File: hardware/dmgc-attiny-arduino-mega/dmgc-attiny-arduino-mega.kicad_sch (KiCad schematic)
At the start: 36 parts, among them J1 Power, J2 Analog, J3 Analog, J4 Digital, J5 PWM, J6 PWM, J7 Communication, SW1 Toggle Flash / Run, SW2 SELECT, SW3 RIGHT, SW4 LEFT, SW5 PUSH, SW6 START/RESET, U1 ATtiny85-20P, U2 Mutex

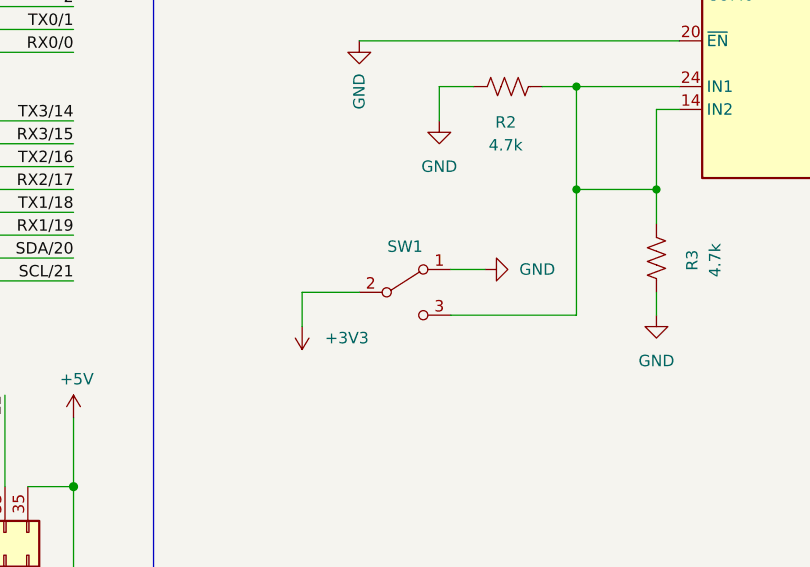
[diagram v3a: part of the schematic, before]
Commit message: Updated gerbers to v0.4, fixed switch problem with pins reversed. Moved C2 to a better location. Added labels for switch.
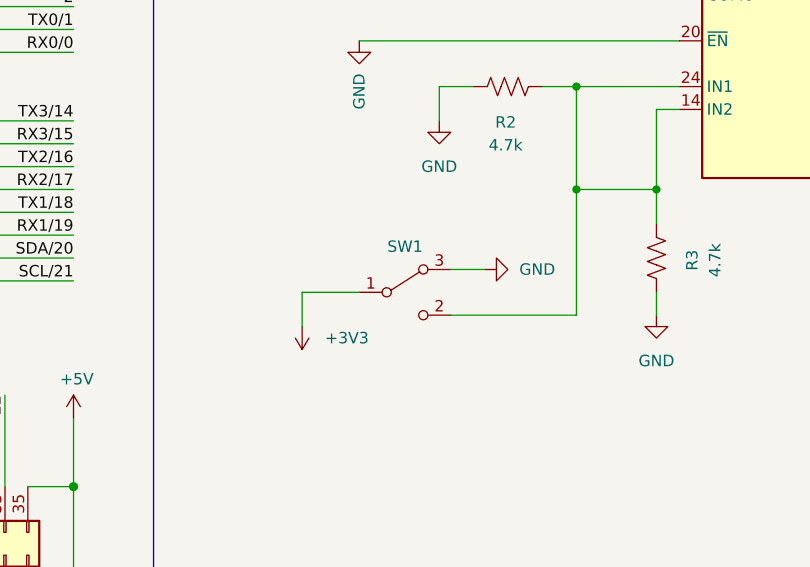
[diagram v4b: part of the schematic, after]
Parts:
- C1, C2, C3: footprint Capacitor_SMD:C_0201_0603Metric -> Capacitor_SMD:C_0603_1608Metric
- R1, R10, R2, R3, R4, R5, R6, R7, R8, R9: footprint Resistor_SMD:R_0201_0603Metric -> Resistor_SMD:R_0603_1608Metric
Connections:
- net +3V3: now also SW1.1 (B); no longer SW1.2 (B)
- net GND: now also SW1.3 (A); no longer SW1.1 (A)
- net at R2.2, R3.2, U2.14 (IN2)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: now also SW1.2 (C); no longer SW1.3 (C)
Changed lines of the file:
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@@
     (title "DMGC Arduino Mega 2650 Shield")
     (date "mar. 31 mars 2015")
-    (rev "0.2")
+    (rev "0.4")
     (company "Author: juvinious")
   )
@@
     (property "Reference" "C1" (id 0) (at 24.13 78.74 0))
     (property "Value" "10uf" (id 1) (at 24.13 81.28 0))
-    (property "Footprint" "Capacitor_SMD:C_0201_0603Metric" (id 2) (at 19.05 80.01 0)
+    (property "Footprint" "Capacitor_SMD:C_0603_1608Metric" (id 2) (at 19.05 80.01 0)
       (effects (font (size 1.27 1.27)) hide)
     )
@@
     (property "Reference" "R7" (id 0) (at 258.0543 87.4665 90))
     (property "Value" "4.7k" (id 1) (at 258.0543 84.9265 90))
-    (property "Footprint" "Resistor_SMD:R_0201_0603Metric" (id 2) (at 257.556 92.456 90)
+    (property "Footprint" "Resistor_SMD:R_0603_1608Metric" (id 2) (at 257.556 92.456 90)
       (effects (font (size 1.27 1.27)) hide)
     )
@@
     (property "Reference" "R5" (id 0) (at 207.2543 117.9465 90))
     (property "Value" "50" (id 1) (at 207.2543 115.4065 90))
-    (property "Footprint" "Resistor_SMD:R_0201_0603Metric" (id 2) (at 206.756 122.936 90)
+    (property "Footprint" "Resistor_SMD:R_0603_1608Metric" (id 2) (at 206.756 122.936 90)
       (effects (font (size 1.27 1.27)) hide)
     )
@@
     (property "Reference" "R9" (id 0) (at 258.0543 128.1065 90))
     (property "Value" "4.7k" (id 1) (at 258.0543 125.5665 90))
-    (property "Footprint" "Resistor_SMD:R_0201_0603Metric" (id 2) (at 257.556 133.096 90)
+    (property "Footprint" "Resistor_SMD:R_0603_1608Metric" (id 2) (at 257.556 133.096 90)
       (effects (font (size 1.27 1.27)) hide)
     )
@@
       (effects (font (size 1.27 1.27)) (justify right))
     )
-    (property "Footprint" "Resistor_SMD:R_0201_0603Metric" (id 2) (at 95.504 39.116 90)
+    (property "Footprint" "Resistor_SMD:R_0603_1608Metric" (id 2) (at 95.504 39.116 90)
       (effects (font (size 1.27 1.27)) hide)
     )
@@
     (property "Reference" "R8" (id 0) (at 258.0543 107.7865 90))
     (property "Value" "4.7k" (id 1) (at 258.0543 105.2465 90))
-    (property "Footprint" "Resistor_SMD:R_0201_0603Metric" (id 2) (at 257.556 112.776 90)
+    (property "Footprint" "Resistor_SMD:R_0603_1608Metric" (id 2) (at 257.556 112.776 90)
       (effects (font (size 1.27 1.27)) hide)
     )
@@
   )
   (symbol (lib_id "power:+3V3") (at 101.6 143.51 180) (unit 1)
-    (in_bom yes) (on_board yes) (fields_autoplaced)
+    (in_bom yes) (on_board yes)
     (property "Reference" "#PWR0103" (id 0) (at 101.6 139.7 0)
       (effects (font (size 1.27 1.27)) hide)
@@
     (property "Reference" "R3" (id 0) (at 144.9435 136.1343 90))
     (property "Value" "4.7k" (id 1) (at 147.4835 136.1343 90))
-    (property "Footprint" "Resistor_SMD:R_0201_0603Metric" (id 2) (at 139.954 135.636 90)
+    (property "Footprint" "Resistor_SMD:R_0603_1608Metric" (id 2) (at 139.954 135.636 90)
       (effects (font (size 1.27 1.27)) hide)
     )
@@
     (property "Reference" "R6" (id 0) (at 258.0543 67.1465 90))
     (property "Value" "4.7k" (id 1) (at 258.0543 64.6065 90))
-    (property "Footprint" "Resistor_SMD:R_0201_0603Metric" (id 2) (at 257.556 72.136 90)
+    (property "Footprint" "Resistor_SMD:R_0603_1608Metric" (id 2) (at 257.556 72.136 90)
       (effects (font (size 1.27 1.27)) hide)
     )
@@
       (effects (font (size 1.27 1.27)) hide)
     )
-    (pin "1")
-    (pin "2")
-    (pin "3")
+    (pin "3")
+    (pin "2")
+    (pin "1")
   )
   (symbol (lib_id "power:GND") (at 140.97 142.24 0) (unit 1)
@@
     (property "Reference" "C2" (id 0) (at 156.21 73.025 0))
     (property "Value" "100n" (id 1) (at 156.21 75.565 0))
-    (property "Footprint" "Capacitor_SMD:C_0201_0603Metric" (id 2) (at 149.86 74.93 0)
+    (property "Footprint" "Capacitor_SMD:C_0603_1608Metric" (id 2) (at 149.86 74.93 0)
       (effects (font (size 1.27 1.27)) hide)
     )
@@
     (property "Reference" "R4" (id 0) (at 199.6343 115.4065 90))
     (property "Value" "50" (id 1) (at 199.6343 112.8665 90))
-    (property "Footprint" "Resistor_SMD:R_0201_0603Metric" (id 2) (at 199.136 120.396 90)
+    (property "Footprint" "Resistor_SMD:R_0603_1608Metric" (id 2) (at 199.136 120.396 90)
       (effects (font (size 1.27 1.27)) hide)
     )
@@
     (property "Reference" "R10" (id 0) (at 258.0543 149.6965 90))
     (property "Value" "4.7k" (id 1) (at 258.0543 147.1565 90))
-    (property "Footprint" "Resistor_SMD:R_0201_0603Metric" (id 2) (at 257.556 154.686 90)
+    (property "Footprint" "Resistor_SMD:R_0603_1608Metric" (id 2) (at 257.556 154.686 90)
       (effects (font (size 1.27 1.27)) hide)
     )
@@
     (property "Reference" "C3" (id 0) (at 169.545 77.47 90))
     (property "Value" "100n" (id 1) (at 169.545 80.01 90))
-    (property "Footprint" "Capacitor_SMD:C_0201_0603Metric" (id 2) (at 170.18 85.09 0)
+    (property "Footprint" "Capacitor_SMD:C_0603_1608Metric" (id 2) (at 170.18 85.09 0)
       (effects (font (size 1.27 1.27)) hide)
     )
@@
     (property "Reference" "R2" (id 0) (at 124.2157 120.8135 90))
     (property "Value" "4.7k" (id 1) (at 124.2157 123.3535 90))
-    (property "Footprint" "Resistor_SMD:R_0201_0603Metric" (id 2) (at 124.714 115.824 90)
+    (property "Footprint" "Resistor_SMD:R_0603_1608Metric" (id 2) (at 124.714 115.824 90)
       (effects (font (size 1.27 1.27)) hide)
     )
@@
     )
     (path "/0e0061c4-c82a-4251-b6cf-a013d6d34bff"
-      (reference "C1") (unit 1) (value "10uf") (footprint "Capacitor_SMD:C_0201_0603Metric")
+      (reference "C1") (unit 1) (value "10uf") (footprint "Capacitor_SMD:C_0603_1608Metric")
     )
     (path "/c02eb7a4-6ea8-413d-938a-576eaf547bdc"
-      (reference "C2") (unit 1) (value "100n") (footprint "Capacitor_SMD:C_0201_0603Metric")
+      (reference "C2") (unit 1) (value "100n") (footprint "Capacitor_SMD:C_0603_1608Metric")
     )
     (path "/e7a9c8c7-1a92-4ce0-bc43-bb567b00e464"
-      (reference "C3") (unit 1) (value "100n") (footprint "Capacitor_SMD:C_0201_0603Metric")
+      (reference "C3") (unit 1) (value "100n") (footprint "Capacitor_SMD:C_0603_1608Metric")
     )
     (path "/797a0085-21e6-4332-a195-a34d527e7d97"
@@
     )
     (path "/3e8ae448-0aeb-4af0-a3bb-3113199e28f3"
-      (reference "R1") (unit 1) (value "510") (footprint "Resistor_SMD:R_0201_0603Metric")
+      (reference "R1") (unit 1) (value "510") (footprint "Resistor_SMD:R_0603_1608Metric")
     )
     (path "/fd673a99-17d1-4a93-ae31-7d19d63fb52c"
-      (reference "R2") (unit 1) (value "4.7k") (footprint "Resistor_SMD:R_0201_0603Metric")
+      (reference "R2") (unit 1) (value "4.7k") (footprint "Resistor_SMD:R_0603_1608Metric")
     )
     (path "/5ce06765-e608-44f6-ae0b-7ed0276423bd"
-      (reference "R3") (unit 1) (value "4.7k") (footprint "Resistor_SMD:R_0201_0603Metric")
+      (reference "R3") (unit 1) (value "4.7k") (footprint "Resistor_SMD:R_0603_1608Metric")
     )
     (path "/d48d9a66-2e68-4a55-a05b-270950f3c5f3"
-      (reference "R4") (unit 1) (value "50") (footprint "Resistor_SMD:R_0201_0603Metric")
+      (reference "R4") (unit 1) (value "50") (footprint "Resistor_SMD:R_0603_1608Metric")
     )
     (path "/1561b2b1-e43b-4156-9baf-35ac6c7857c9"
-      (reference "R5") (unit 1) (value "50") (footprint "Resistor_SMD:R_0201_0603Metric")
+      (reference "R5") (unit 1) (value "50") (footprint "Resistor_SMD:R_0603_1608Metric")
     )
     (path "/b0c07ccb-e416-475c-af18-fc635e5976c7"
-      (reference "R6") (unit 1) (value "4.7k") (footprint "Resistor_SMD:R_0201_0603Metric")
+      (reference "R6") (unit 1) (value "4.7k") (footprint "Resistor_SMD:R_0603_1608Metric")
     )
     (path "/12fc2809-8203-43d5-ae46-8ba6dd72ebfa"
-      (reference "R7") (unit 1) (value "4.7k") (footprint "Resistor_SMD:R_0201_0603Metric")
+      (reference "R7") (unit 1) (value "4.7k") (footprint "Resistor_SMD:R_0603_1608Metric")
     )
     (path "/40a587cf-4d85-49d5-9f62-e3bd9458bbc5"
-      (reference "R8") (unit 1) (value "4.7k") (footprint "Resistor_SMD:R_0201_0603Metric")
+      (reference "R8") (unit 1) (value "4.7k") (footprint "Resistor_SMD:R_0603_1608Metric")
     )
     (path "/2d3682de-db88-46bc-b411-eabada1c3856"
-      (reference "R9") (unit 1) (value "4.7k") (footprint "Resistor_SMD:R_0201_0603Metric")
+      (reference "R9") (unit 1) (value "4.7k") (footprint "Resistor_SMD:R_0603_1608Metric")
     )
     (path "/dceb228b-32c7-41d9-8350-1eb03b8b1d23"
-      (reference "R10") (unit 1) (value "4.7k") (footprint "Resistor_SMD:R_0201_0603Metric")
+      (reference "R10") (unit 1) (value "4.7k") (footprint "Resistor_SMD:R_0603_1608Metric")
     )
     (path "/b3039fe5-e1fa-4708-9b71-287e276d5974"
